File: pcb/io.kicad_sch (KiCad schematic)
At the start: 3 parts, among them J601 Conn_01x16, J602 Conn_01x14, J603 Conn_01x03

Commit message: add footprints
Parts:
- J601: footprint (none) -> Connector_PinHeader_2.54mm:PinHeader_1x16_P2.54mm_Vertical
- J603: footprint (none) -> Connector_PinHeader_2.54mm:PinHeader_1x03_P2.54mm_Vertical
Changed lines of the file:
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@@
 			)
 		)
-		(property "Footprint" ""
+		(property "Footprint" "Connector_PinHeader_2.54mm:PinHeader_1x16_P2.54mm_Vertical"
 			(at 107.95 45.72 0)
 			(effects
@@
 			)
 		)
-		(property "Footprint" ""
+		(property "Footprint" "Connector_PinHeader_2.54mm:PinHeader_1x03_P2.54mm_Vertical"
 			(at 168.91 62.23 0)
 			(effects

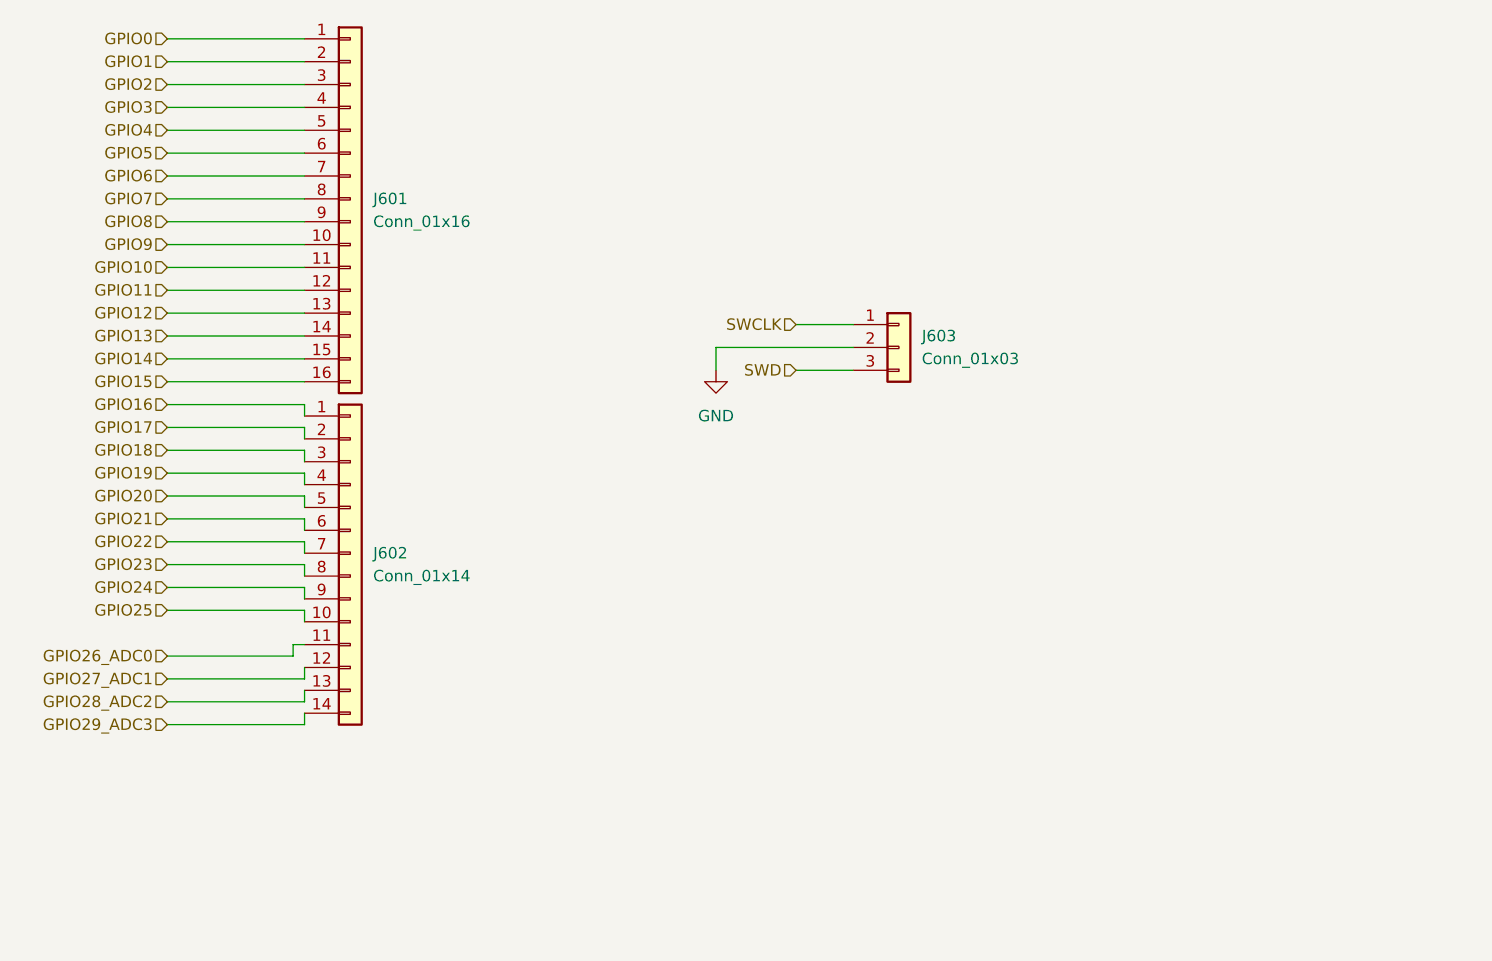
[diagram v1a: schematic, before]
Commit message: add footprints + expose grounds and power on pins
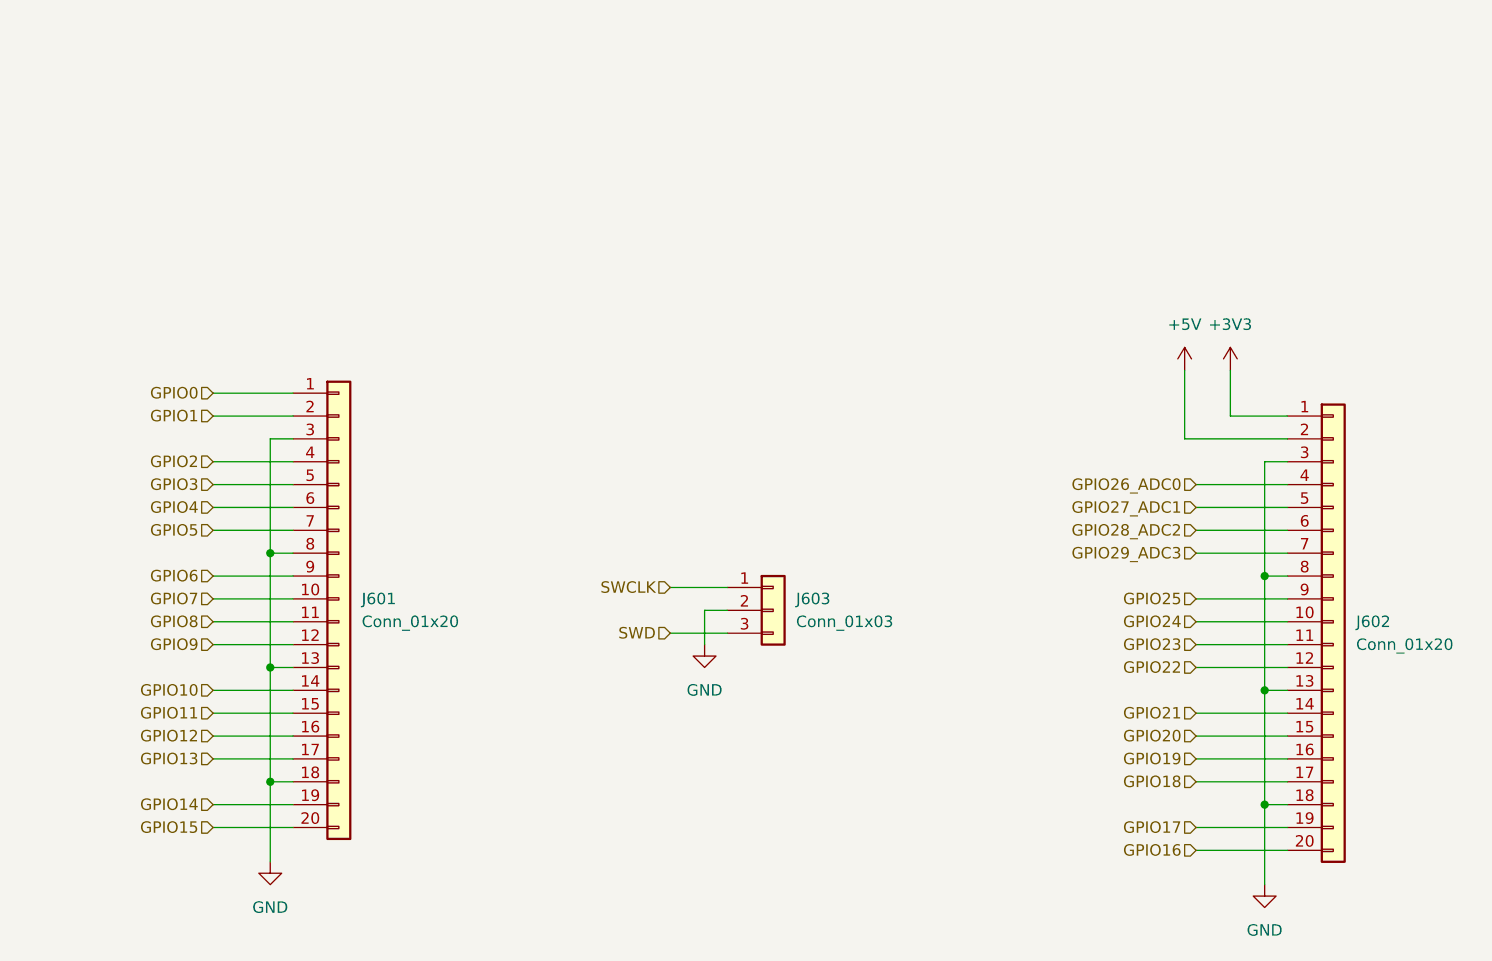
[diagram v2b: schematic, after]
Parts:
- removed J601: Conn_01x16, Connector_PinHeader_2.54mm:PinHeader_1x16_P2.54mm_Vertical, symbol Connector_Generic:Conn_01x16
- removed J602: Conn_01x14, symbol Connector_Generic:Conn_01x14
- added J601, J602: Conn_01x20, Connector_PinHeader_2.54mm:PinHeader_1x20_P2.54mm_Vertical, symbol Connector_Generic:Conn_01x20
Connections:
- net GND: now also J601.13 (Pin_13), J601.18 (Pin_18), J601.3 (Pin_3), J601.8 (Pin_8), J602.13 (Pin_13), J602.18 (Pin_18), J602.3 (Pin_3), J602.8 (Pin_8)
- net GPIO0: now also J601.1 (Pin_1)
- net GPIO1: now also J601.2 (Pin_2)
- net GPIO10: now also J601.14 (Pin_14)
- net GPIO11: now also J601.15 (Pin_15)
- net GPIO12: now also J601.16 (Pin_16)
- net GPIO13: now also J601.17 (Pin_17)
- net GPIO14: now also J601.19 (Pin_19)
- net GPIO15: now also J601.20 (Pin_20)
- net GPIO16: now also J602.20 (Pin_20)
- net GPIO17: now also J602.19 (Pin_19)
- net GPIO18: now also J602.17 (Pin_17)
- net GPIO19: now also J602.16 (Pin_16)
- net GPIO2: now also J601.4 (Pin_4)
- net GPIO20: now also J602.15 (Pin_15)
- net GPIO21: now also J602.14 (Pin_14)
- net GPIO22: now also J602.12 (Pin_12)
- net GPIO23: now also J602.11 (Pin_11)
- net GPIO24: now also J602.10 (Pin_10)
- net GPIO25: now also J602.9 (Pin_9)
- net GPIO26_ADC0: now also J602.4 (Pin_4)
- net GPIO27_ADC1: now also J602.5 (Pin_5)
- net GPIO28_ADC2: now also J602.6 (Pin_6)
- net GPIO29_ADC3: now also J602.7 (Pin_7)
- net GPIO3: now also J601.5 (Pin_5)
- net GPIO4: now also J601.6 (Pin_6)
- net GPIO5: now also J601.7 (Pin_7)
- net GPIO6: now also J601.9 (Pin_9)
- net GPIO7: now also J601.10 (Pin_10)
- net GPIO8: now also J601.11 (Pin_11)
- net GPIO9: now also J601.12 (Pin_12)
- new net +3V3: J602.1 (Pin_1)
- new net +5V: J602.2 (Pin_2)
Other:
- moved on the sheet: J603

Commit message: wip pcb placement
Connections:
- net GPIO26_ADC0: now also J602.7 (Pin_7); no longer J602.4 (Pin_4)
- net GPIO27_ADC1: now also J602.6 (Pin_6); no longer J602.5 (Pin_5)
- net GPIO28_ADC2: now also J602.5 (Pin_5); no longer J602.6 (Pin_6)
- net GPIO29_ADC3: now also J602.4 (Pin_4); no longer J602.7 (Pin_7)
